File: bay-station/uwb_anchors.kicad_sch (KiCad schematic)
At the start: 28 parts, among them U4 DWM3000, U5 DWM3000, U6 DWM3000, U7 DWM3000

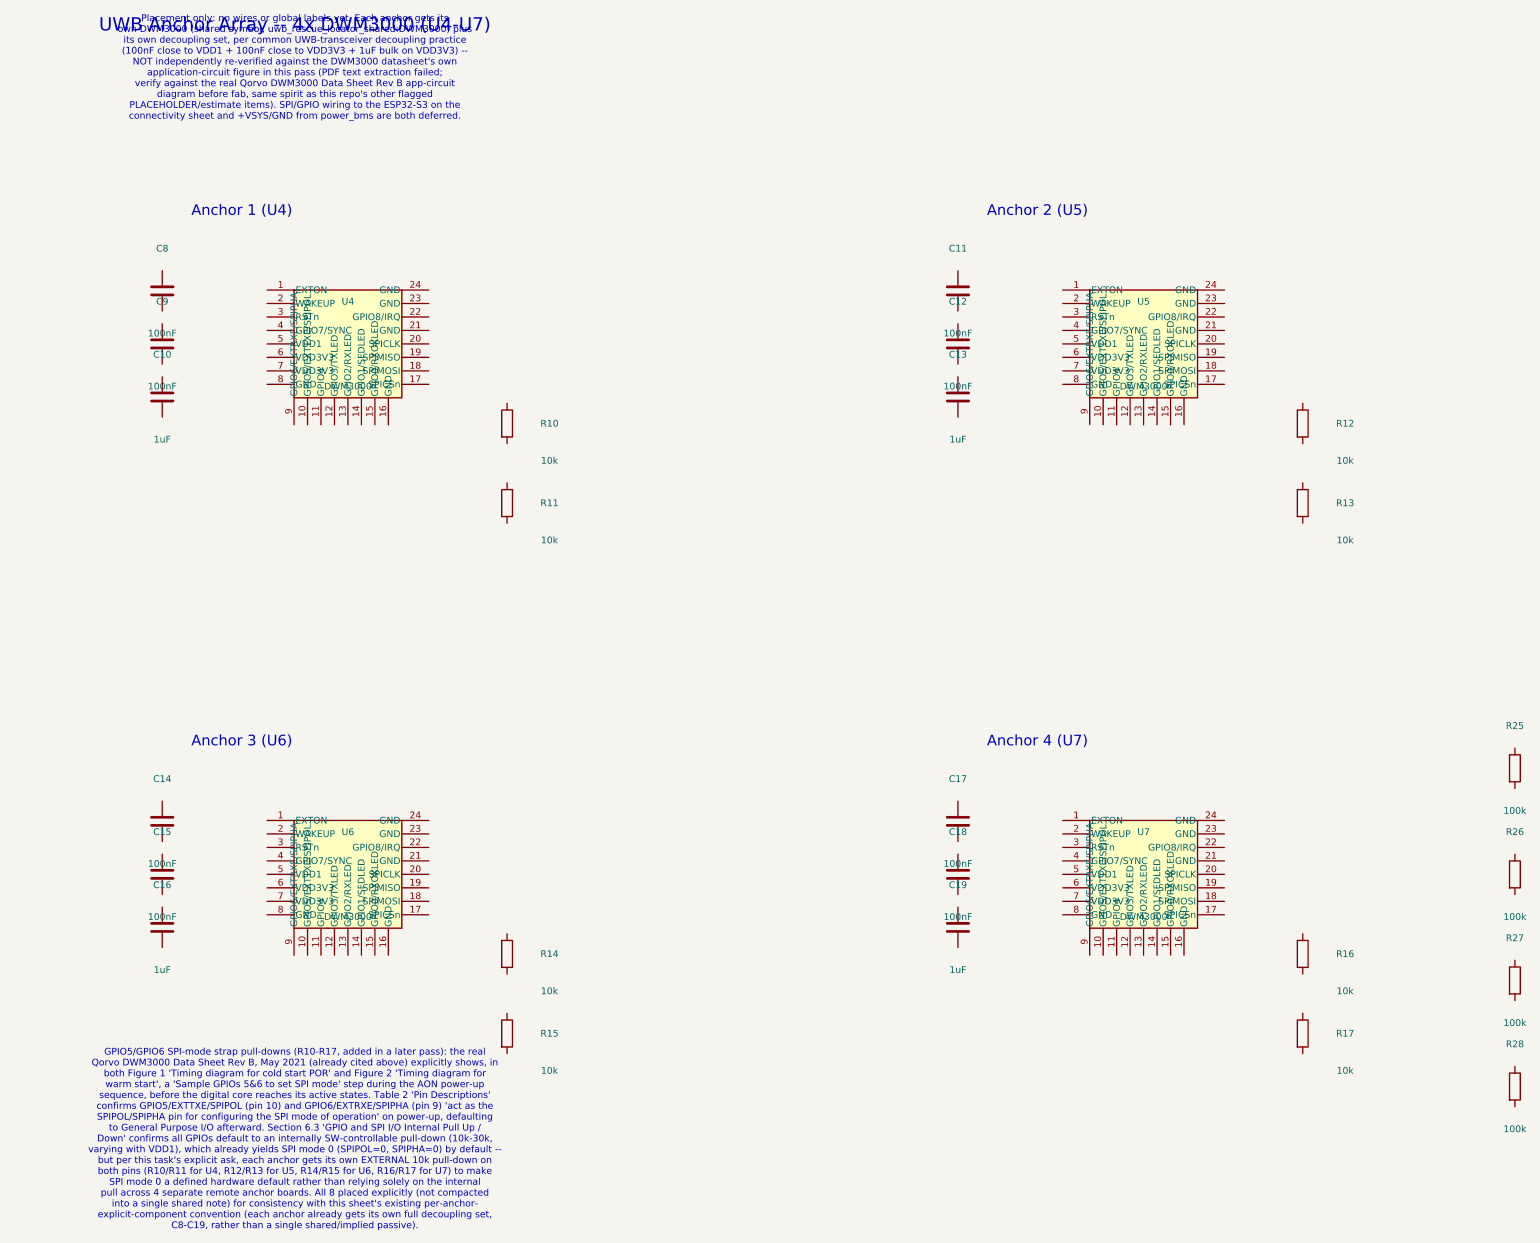
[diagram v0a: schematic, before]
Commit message: Make schematics readable: wire stubs, A3 reflow, DWM3000 symbol redraw
Connectivity is unchanged -- verified by diffing the exported netlist against
the previous commit: 34 nets, identical pin membership on every one. This is
presentation only.

The problem was pre-existing, not new. Labels were placed exactly on the pin
endpoint, so label text printed on top of the symbol's own pin name (+3V3
stamped over VCC, UWB_CS over GPIO_1). power_bms had it on U1/U2/Q2 as well;
it only became obvious when the convention was scaled onto a 55-pin part.
Every label now sits at the end of a short wire stub pointing away from the
body, which is the standard KiCad idiom.

DWM3000 symbol redrawn (shared/symbols/)
- The old symbol was a 20mm square carrying pin names like GPIO0/RXOKLED drawn
  vertically along the bottom edge, where they collided with each other inside
  the symbol. No amount of label placement fixes that.
- Now 56 x 41mm, functionally grouped: power/ground/control left, SPI/GPIO
  right, no bottom-edge pins. All 24 pins and every property preserved.
- Checked the blast radius before touching it: bay-station is entirely unwired
  (0 wires, 0 labels on every sheet), so nothing was orphaned. Its cached copy
  is refreshed here and its netlist still exports cleanly at 75 components.

Layout
- radio_mcu and power_bms moved to A3 and reflowed into functional blocks;
  42 symbols repositioned.
- 38 annotations added, carrying the datasheet citations and reasoning that
  previously lived only in the markdown -- LFXO load-cap derivation, the
  ~2.1uA battery-divider tradeoff, why DW01A's GND sits on CELL_N, the LDO
  headroom budget, and the unchanged-from-NINA-B111 SWD pin numbers.

Verification
- Wrote a text-collision checker rather than eyeballing it. It caught two
  classes of bug: duplicated annotations (strip() cleared labels and wires but
  not text, so a second pass layered notes over old ones) and doubled labels on
  stacked same-net pins (USB-C J1 A9/B9, A12/B12;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
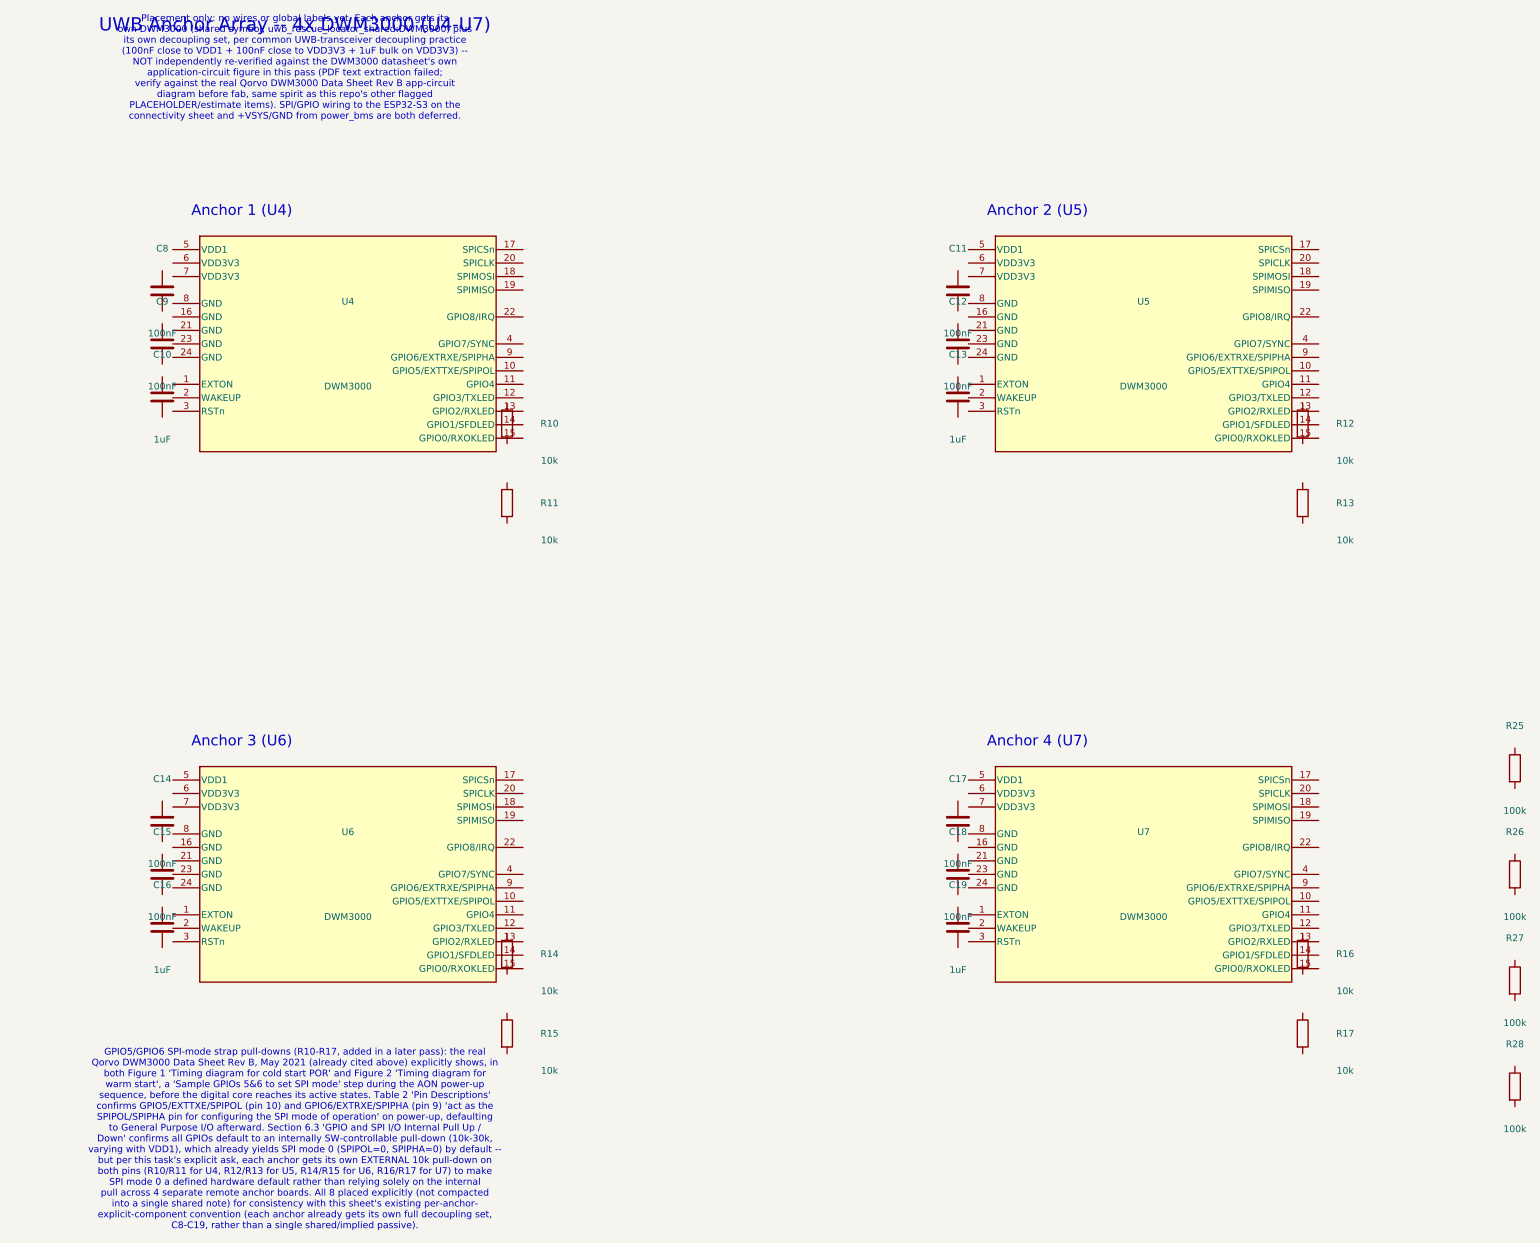
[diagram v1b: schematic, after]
